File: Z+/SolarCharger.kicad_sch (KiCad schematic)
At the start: 25 parts, among them U8 ADM1176-1ARMZ-R7

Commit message: Z+ updates WIP
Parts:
- SC1: renamed from SC7; footprint SolarPanels:SM141K06TF -> Argus-Miscellaneous:SM141K06TF
- SC2: renamed from SC8; footprint SolarPanels:SM141K06TF -> Argus-Miscellaneous:SM141K06TF
- SC3: renamed from SC9; footprint SolarPanels:SM141K06TF -> Argus-Miscellaneous:SM141K06TF
- SC4: renamed from SC10; footprint SolarPanels:SM141K06TF -> Argus-Miscellaneous:SM141K06TF
- SC5: renamed from SC11; footprint SolarPanels:SM141K06TF -> Argus-Miscellaneous:SM141K06TF
- SC6: renamed from SC12; footprint SolarPanels:SM141K06TF -> Argus-Miscellaneous:SM141K06TF
- U8: symbol Mainboard:ADM1176-1ARMZ-R7 -> Argus-IC:ADM1176-1ARMZ-R7
- renumbered C41 to C17, D15 to D10, D10 to D5, D11 to D6, D12 to D7, D13 to D8, D14 to D9, F4 to F7, R1 to R48, R2 to R49, R3 to R50, R4 to R51, R58 to R52, R59 to R53, R73 to R54, R104 to R55, R105 to R56, R106 to R57

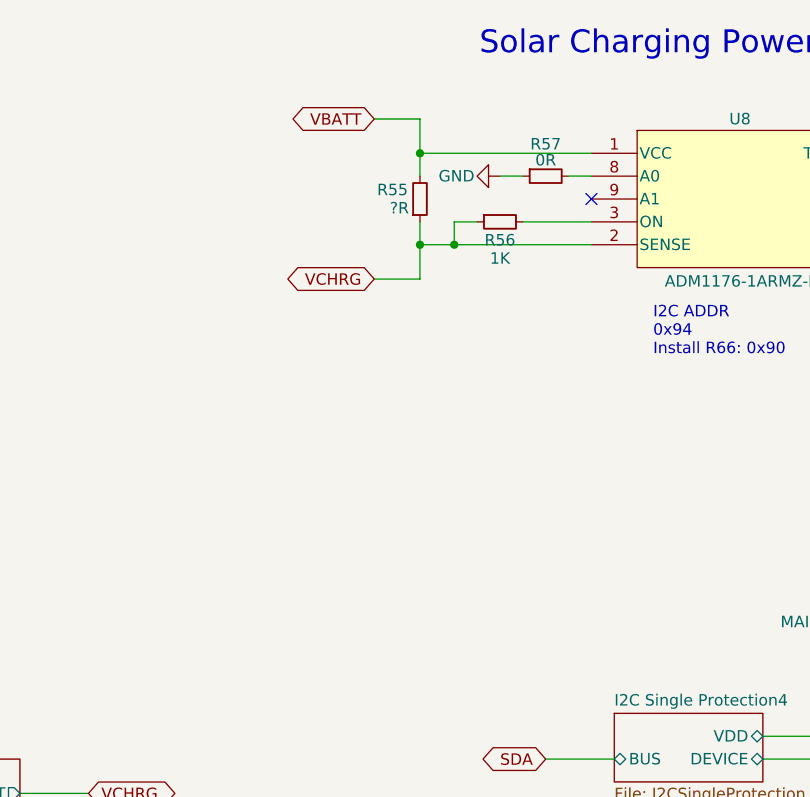
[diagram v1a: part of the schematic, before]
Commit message: Placed all components
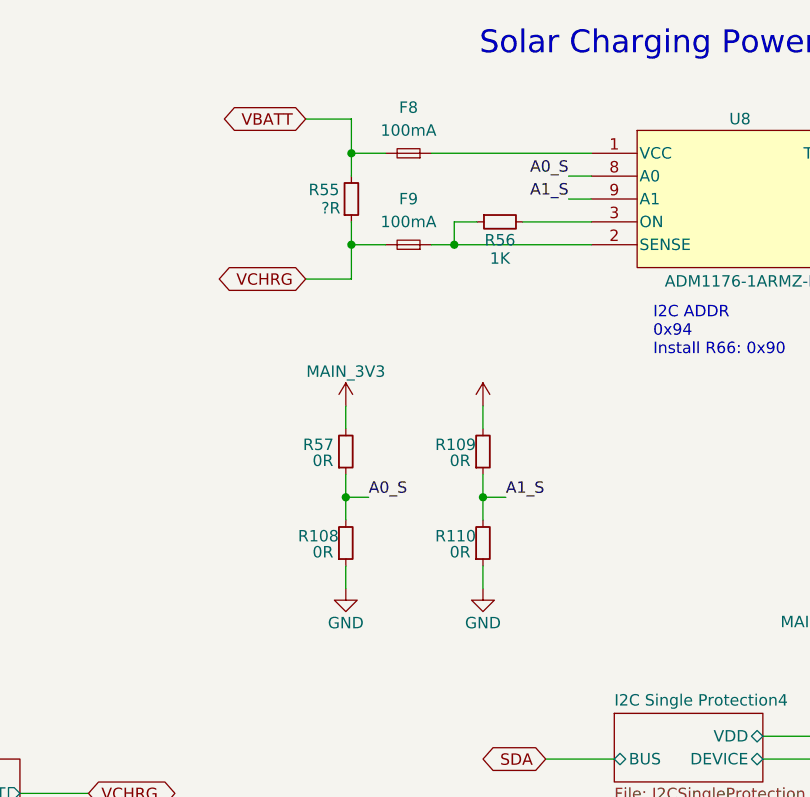
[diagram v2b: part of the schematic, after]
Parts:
- added F8, F9: 100mA, Fuse:Fuse_0603_1608Metric, symbol Device:Fuse_Small
- added R108, R109, R110: 0R, Resistor_SMD:R_0603_1608Metric, symbol Device:R_Small
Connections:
- net GND: now also R108.1, R110.1; no longer R57.1
- net MAIN_3V3: now also R57.2, R109.2
- net VBATT: now also F8.2; no longer U8.1 (VCC)
- net VCHRG: now also F9.2; no longer R56.1, U8.2 (SENSE)
- net A0_S: now reaches U8.8 (A0)
- net A0_S: now also R57.1, R108.2; no longer R57.2
- net A1_S: now reaches U8.9 (A1)
- net A1_S: now also R109.1, R110.2
- new net: F9.1, R56.1, U8.2 (SENSE)
- new net: F8.1, U8.1 (VCC)
- no-connect marks 3 -> 2
